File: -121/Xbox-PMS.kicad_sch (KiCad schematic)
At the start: 112 parts, among them IC1 SIC437BED-T1-GE3, IC3 SIC437BED-T1-GE3, IC4 SIC437BED-T1-GE3, J2 USB_C_Receptacle_USB2.0_16P, J3 Jack-DC, J6 Conn_01x04_Pin, J7 Conn_01x04_Pin, U1 TVS2200DRV, U2 TPS25750, U3 CAT24C512

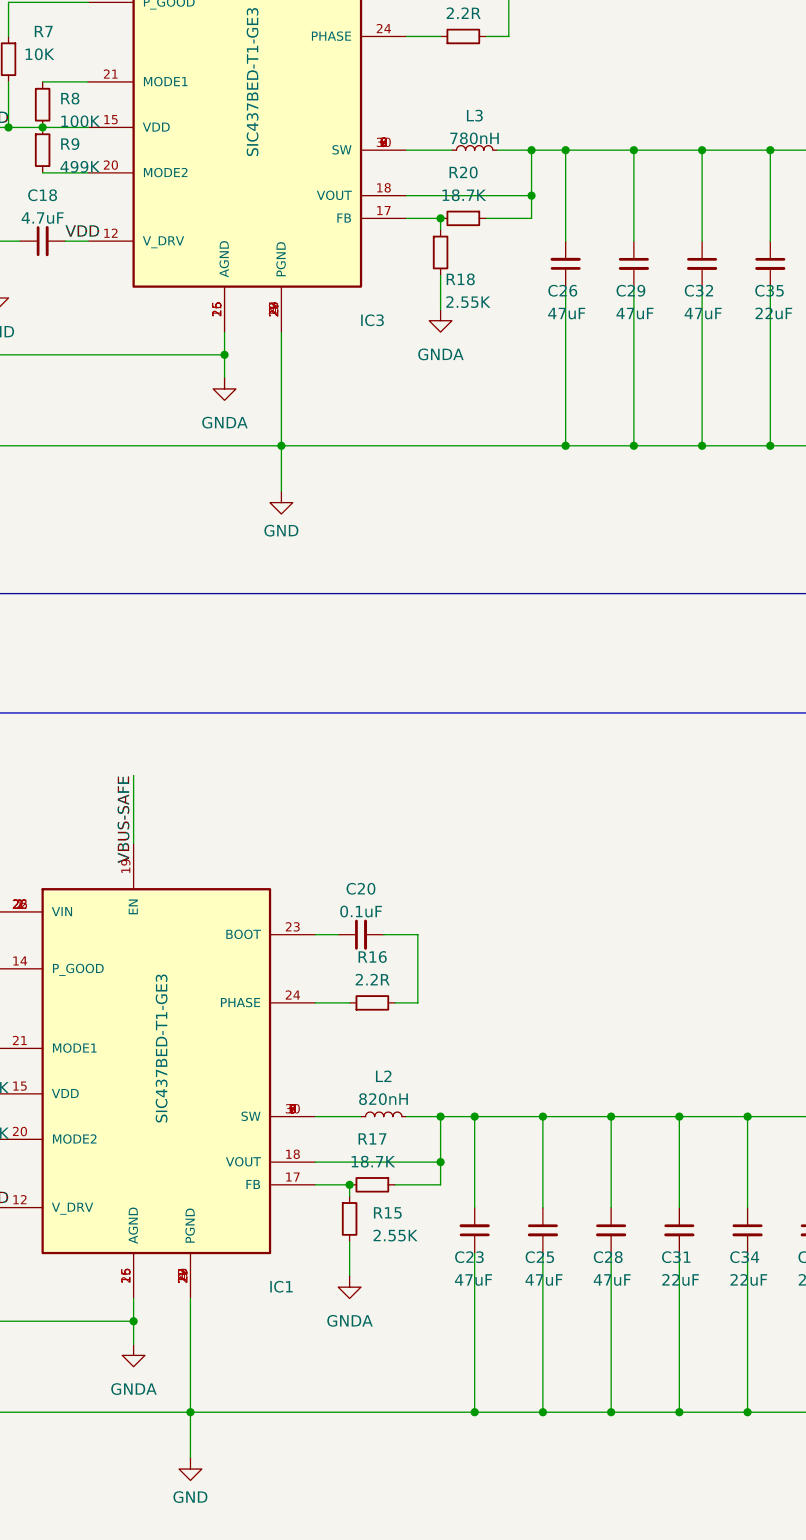
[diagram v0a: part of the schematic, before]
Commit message: Add jumper 0ohm
configurable STANDBY voltage.
update silkscreen
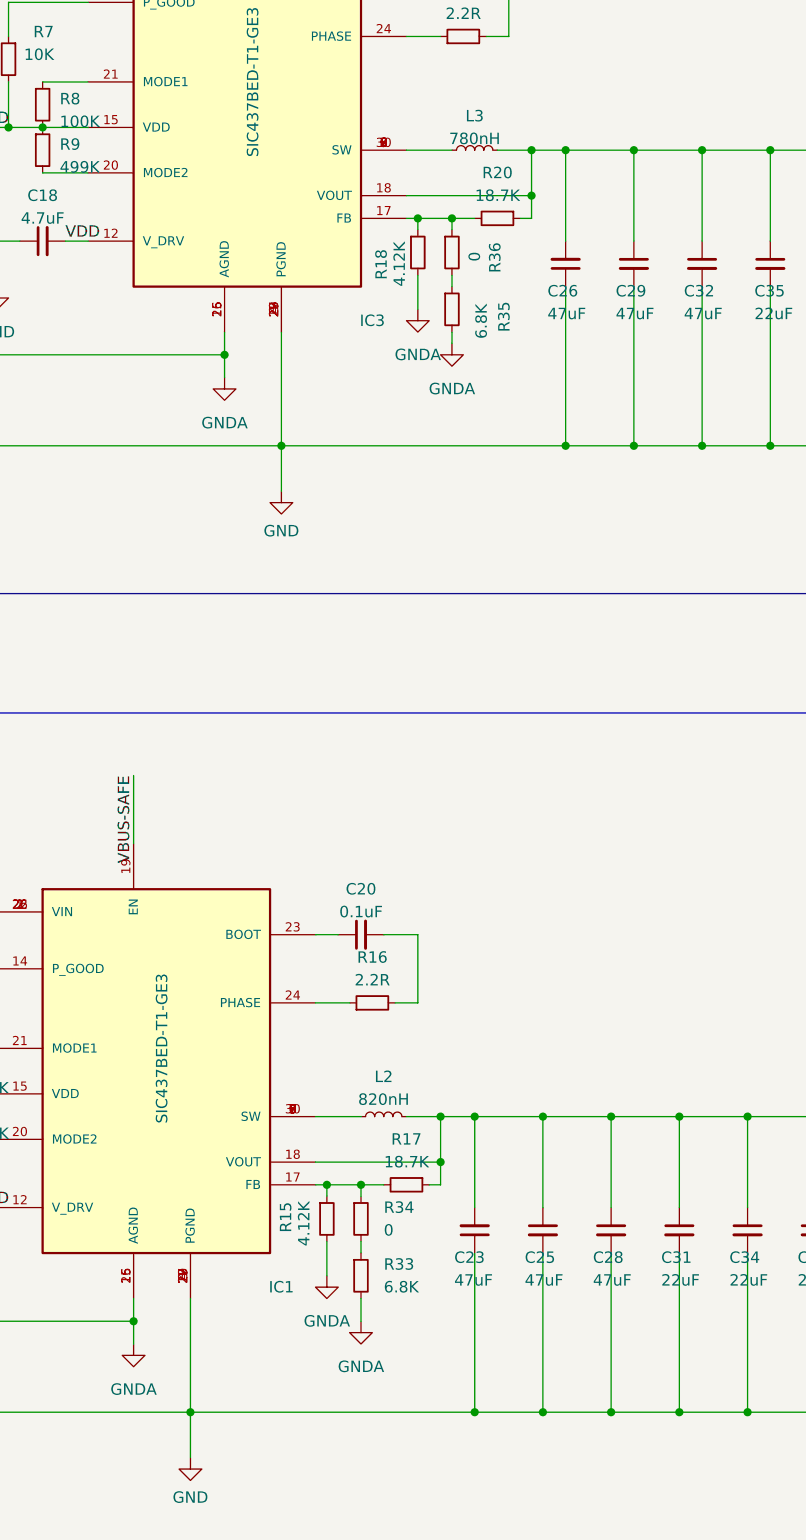
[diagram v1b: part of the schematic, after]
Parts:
- added R33, R35: 6.8K, Resistor_SMD:R_0402_1005Metric, symbol Device:R_Small
- added R34, R36: 0, Resistor_SMD:R_0402_1005Metric, symbol Device:R_Small
- R15, R18: value 2.55K -> 4.12K
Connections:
- net GND: now also R33.2, R35.2
- net at IC3.17 (FB), R18.1, R20.2: now also R36.1
- net at IC1.17 (FB), R15.1, R17.2: now also R34.1
- new net: R33.1, R34.2
- new net: R35.1, R36.2
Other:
- moved on the sheet: R15, R17, R18, R20
